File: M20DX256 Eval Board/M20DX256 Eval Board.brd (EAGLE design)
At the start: 60 x 30 mm, 20 parts, among them J1 M52-040000S0545, J2 20_PIN, J3 20_PIN, SW1 KMR211G, U1 MK20DX256VLH7, Y1 8MHz, Y2 32.768kHz, 12.5pF

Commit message: Place the component on the board
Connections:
- removed net XRES: U1.27
- net DAC0_OUT: now also J2.P$15; no longer J2.P$19
- net PGA0_N: now also J2.P$18; no longer J2.P$17
- net PGA0_P: now also J2.P$19; no longer J2.P$18
- net PGA1_N: now also J2.P$16; no longer J2.P$15
- net PGA1_P: now also J2.P$17; no longer J2.P$16
- net RESET: now also U1.27
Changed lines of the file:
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@@
 <wire x1="29.238" y1="9.3866" x2="52.185" y2="17.54" width="0" layer="19" extent="1-1"/>
-</signal>
-<signal name="XRES">
-<contactref element="U1" pad="27"/>
 </signal>
 <signal name="TMS/SWDIO">
@@
 <signal name="PGA1_N">
 <contactref element="U1" pad="12"/>
-<contactref element="J2" pad="P$15"/>
-<wire x1="18.57" y1="0" x2="24.3866" y2="13.2474" width="0" layer="19" extent="1-1"/>
+<contactref element="J2" pad="P$16"/>
+<wire x1="16.03" y1="0" x2="24.3866" y2="13.2474" width="0" layer="19" extent="1-1"/>
 </signal>
 <signal name="PGA1_P">
 <contactref element="U1" pad="11"/>
-<contactref element="J2" pad="P$16"/>
-<wire x1="16.03" y1="0" x2="24.3866" y2="13.7554" width="0" layer="19" extent="1-1"/>
+<contactref element="J2" pad="P$17"/>
+<wire x1="13.49" y1="0" x2="24.3866" y2="13.7554" width="0" layer="19" extent="1-1"/>
 </signal>
 <signal name="PGA0_N">
 <contactref element="U1" pad="10"/>
-<contactref element="J2" pad="P$17"/>
-<wire x1="13.49" y1="0" x2="24.3866" y2="14.238" width="0" layer="19" extent="1-1"/>
+<contactref element="J2" pad="P$18"/>
+<wire x1="10.95" y1="0" x2="24.3866" y2="14.238" width="0" layer="19" extent="1-1"/>
 </signal>
 <signal name="PGA0_P">
 <contactref element="U1" pad="9"/>
-<contactref element="J2" pad="P$18"/>
-<wire x1="10.95" y1="0" x2="24.3866" y2="14.746" width="0" layer="19" extent="1-1"/>
+<contactref element="J2" pad="P$19"/>
+<wire x1="8.41" y1="0" x2="24.3866" y2="14.746" width="0" layer="19" extent="1-1"/>
 </signal>
 <signal name="N$3">
@@
 <contactref element="SW1" pad="4"/>
 <contactref element="J1" pad="10"/>
+<contactref element="U1" pad="27"/>
 <wire x1="53.34" y1="9.31" x2="52.185" y2="16.27" width="0" layer="19" extent="1-1"/>
 <wire x1="53.34" y1="7.2" x2="53.34" y2="9.31" width="0" layer="19" extent="1-1"/>
@@
 <wire x1="56.4" y1="5.57" x2="53.34" y2="7.2" width="0" layer="19" extent="1-1"/>
 <wire x1="35.6134" y1="11.7488" x2="52.185" y2="16.27" width="0" layer="19" extent="1-1"/>
+<wire x1="31.2446" y1="9.3866" x2="35.6134" y2="11.7488" width="0" layer="19" extent="1-1"/>
 </signal>
 <signal name="N$7">
@@
 <signal name="DAC0_OUT">
 <contactref element="U1" pad="18"/>
-<contactref element="J2" pad="P$19"/>
-<wire x1="8.41" y1="0" x2="26.7488" y2="9.3866" width="0" layer="19" extent="1-1"/>
+<contactref element="J2" pad="P$15"/>
+<wire x1="18.57" y1="0" x2="26.7488" y2="9.3866" width="0" layer="19" extent="1-1"/>
 </signal>
 </signals>

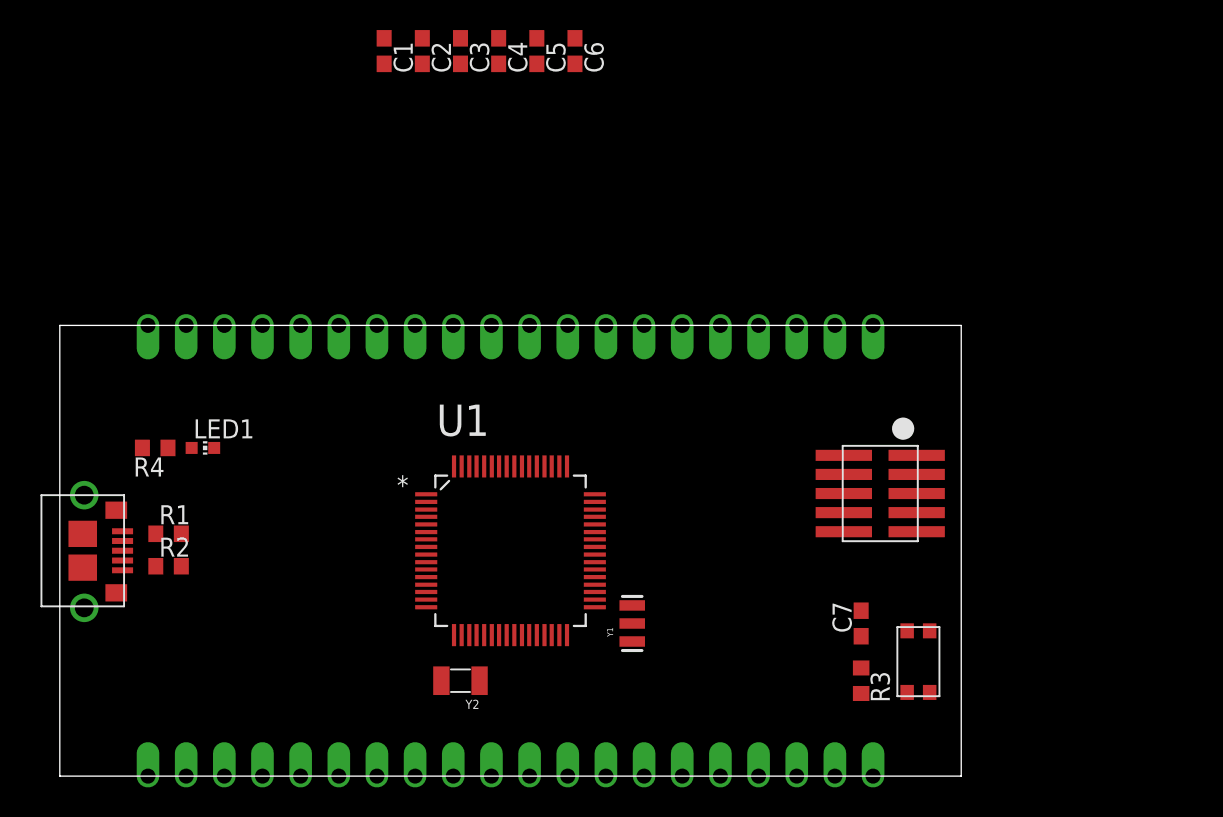
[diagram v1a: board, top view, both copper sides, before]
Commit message: route J3
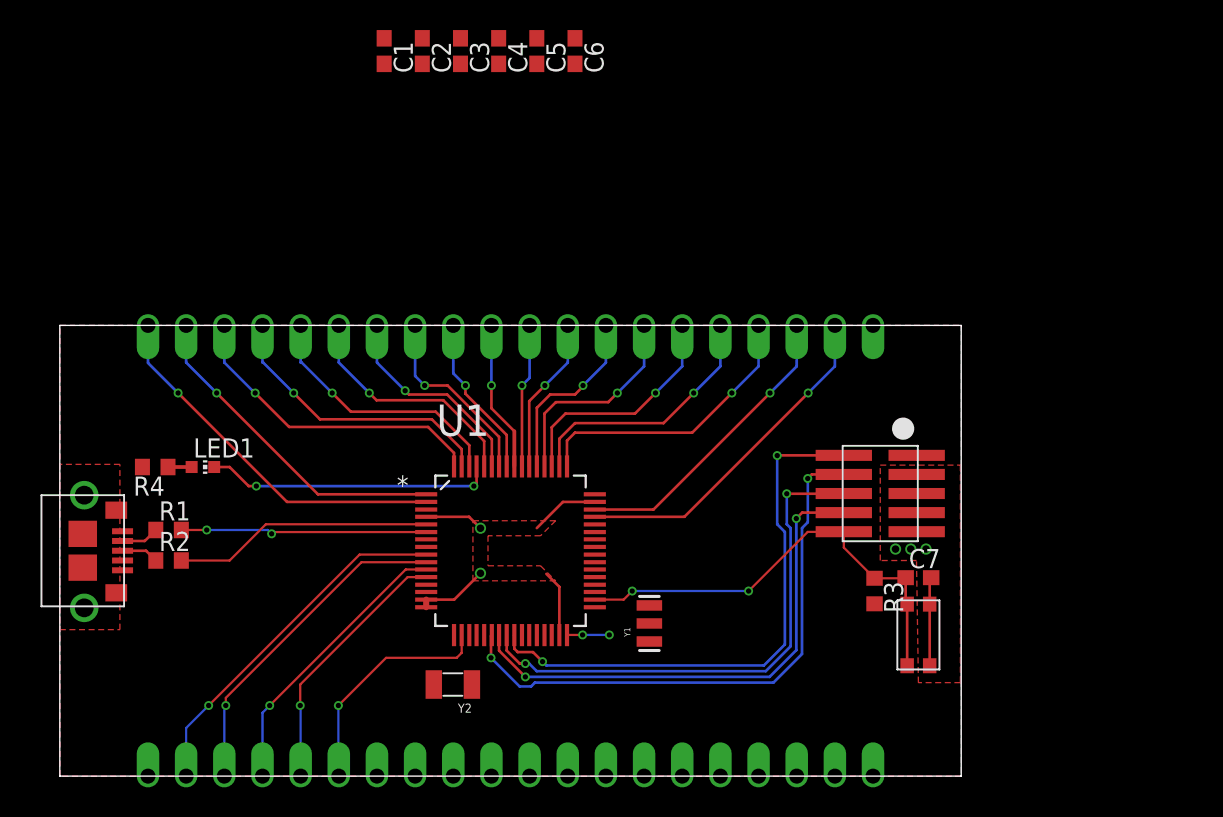
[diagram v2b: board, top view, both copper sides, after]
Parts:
- moved R3 6.03 mm to (54.2, 12.3)
- moved C7 4.88 mm to (57.1, 13.2), turned to 0 degrees
- moved SW1 1.78 mm to (57.1, 9.40)
- moved LED1 1.27 mm to (9.53, 20.6)
- moved R4 1.27 mm to (6.35, 20.6)
- moved Y1 1.14 mm to (39.2, 10.2)
- moved Y2 0.57 mm to (26.2, 6.10)
- moved R2 0.38 mm to (7.24, 14.4)
- moved R1 0.25 mm to (7.24, 16.4)
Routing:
- net TCK/SWDCLK: track 0.00 -> 38.3 mm, vias 0 -> 2
- net TMS/SWDIO: track 0.00 -> 37.2 mm, vias 0 -> 2
- net TDO: track 0.00 -> 35.2 mm, vias 0 -> 2
- net TDI: track 0.00 -> 34.4 mm, vias 0 -> 2
- net RESET: track 0.00 -> 30.4 mm, vias 0 -> 2
- net PTE1: track 0.00 -> 24.8 mm, vias 0 -> 1
- net PGA0_P: track 0.00 -> 24.0 mm, vias 0 -> 1
- net GND: track 0.00 -> 23.7 mm, vias 0 -> 5
- net PTC2: track 0.00 -> 22.8 mm, vias 0 -> 1
- net PGA0_N: track 0.00 -> 22.3 mm, vias 0 -> 1
- net PTE0: track 0.00 -> 22.1 mm, vias 0 -> 1
- net PTD7: track 0.00 -> 21.2 mm, vias 0 -> 1
- net PTC3: track 0.00 -> 20.1 mm, vias 0 -> 1
- net PTD6: track 0.00 -> 19.3 mm, vias 0 -> 1
- net PTC4: track 0.00 -> 19.2 mm, vias 0 -> 1
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- added copper zone on layer 1, net +3V3
- added copper zone on layer 1, net GND
- added copper zone on layer 16, net GND

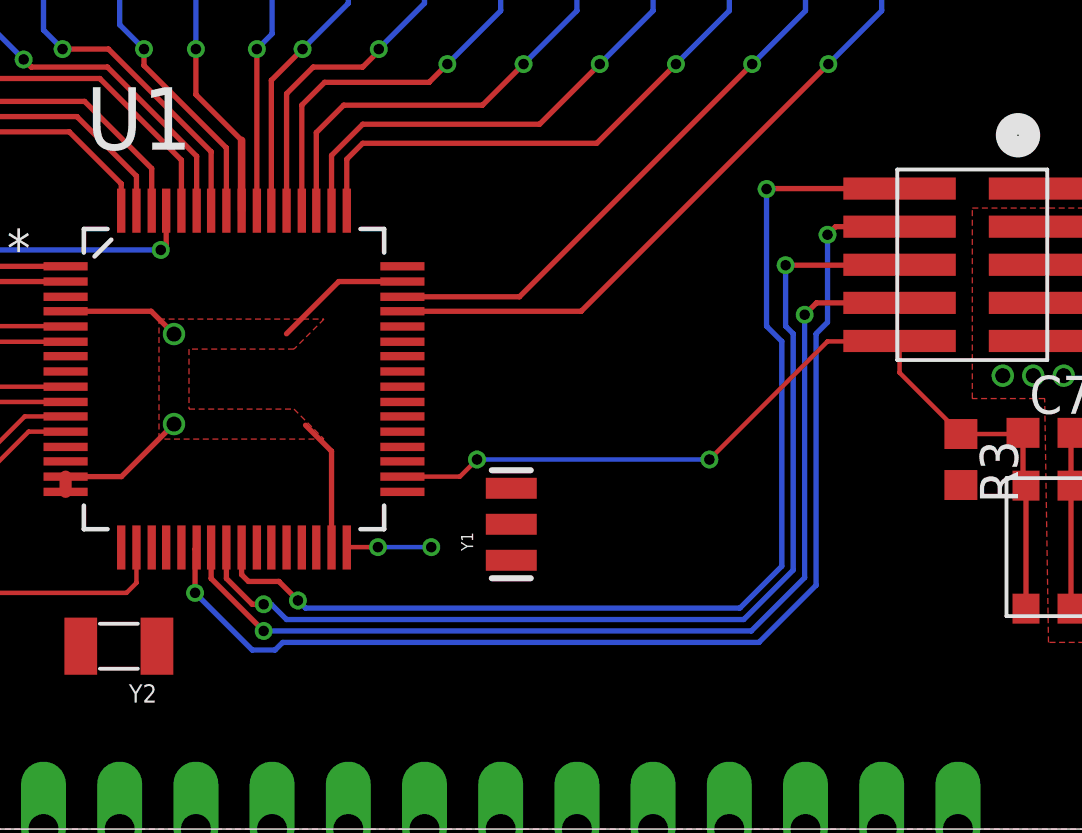
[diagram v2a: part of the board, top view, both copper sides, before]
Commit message: Route J1
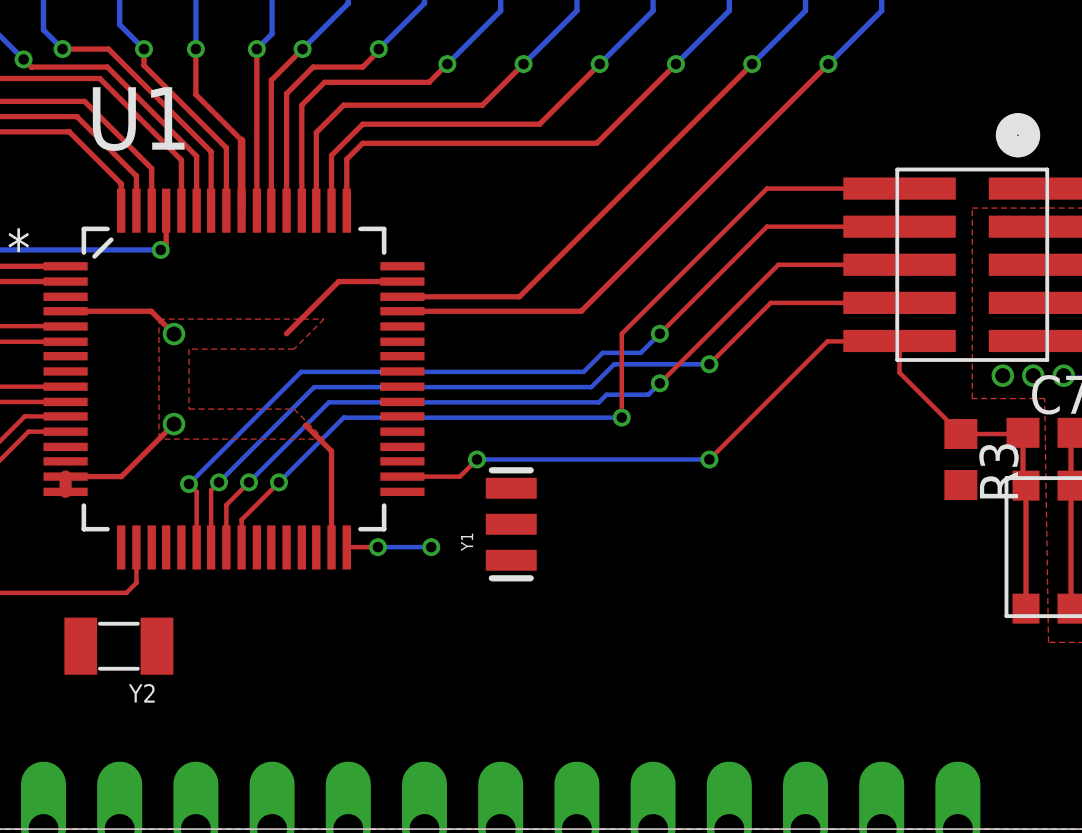
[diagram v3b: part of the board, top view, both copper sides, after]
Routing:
- net TCK/SWDCLK: track 38.3 -> 29.5 mm
- net TMS/SWDIO: track 37.2 -> 29.1 mm
- net TDO: track 35.2 -> 27.2 mm
- net TDI: track 34.4 -> 27.4 mm
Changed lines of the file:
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@@
 <contactref element="J1" pad="4"/>
 <contactref element="U1" pad="22"/>
-<wire x1="52.185" y1="20.08" x2="50.052" y2="20.08" width="0.1778" layer="1"/>
-<wire x1="50.052" y1="20.08" x2="49.784" y2="19.812" width="0.1778" layer="1"/>
-<via x="49.784" y="19.812" extent="1-16" drill="0.35"/>
-<wire x1="30.607" y1="5.969" x2="28.702" y2="7.874" width="0.1778" layer="16"/>
-<via x="28.702" y="7.874" extent="1-16" drill="0.35"/>
-<wire x1="28.702" y1="7.874" x2="28.702" y2="9.3332" width="0.1778" layer="1"/>
-<wire x1="28.702" y1="9.3332" x2="28.7554" y2="9.3866" width="0.1778" layer="1"/>
-<wire x1="49.784" y1="19.812" x2="49.784" y2="16.891" width="0.1778" layer="16"/>
-<wire x1="49.784" y1="16.891" x2="49.403" y2="16.51" width="0.1778" layer="16"/>
-<wire x1="49.403" y1="16.51" x2="49.403" y2="8.128" width="0.1778" layer="16"/>
-<wire x1="49.403" y1="8.128" x2="47.498" y2="6.223" width="0.1778" layer="16"/>
-<wire x1="30.607" y1="5.969" x2="31.369" y2="5.969" width="0.1778" layer="16"/>
-<wire x1="31.369" y1="5.969" x2="31.623" y2="6.223" width="0.1778" layer="16"/>
-<wire x1="31.623" y1="6.223" x2="47.498" y2="6.223" width="0.1778" layer="16"/>
+<via x="28.5" y="11.5" extent="1-16" drill="0.35"/>
+<wire x1="28.7554" y1="9.3866" x2="28.7554" y2="11.2446" width="0.15" layer="1"/>
+<wire x1="28.7554" y1="11.2446" x2="28.5" y2="11.5" width="0.15" layer="1"/>
+<wire x1="28.5" y1="11.5" x2="32.24" y2="15.24" width="0.15" layer="16"/>
+<wire x1="32.24" y1="15.24" x2="41.656" y2="15.24" width="0.15" layer="16"/>
+<via x="44.196" y="16.51" extent="1-16" drill="0.35"/>
+<wire x1="44.196" y1="16.51" x2="47.766" y2="20.08" width="0.15" layer="1"/>
+<wire x1="47.766" y1="20.08" x2="52.185" y2="20.08" width="0.15" layer="1"/>
+<wire x1="41.656" y1="15.24" x2="42.291" y2="15.875" width="0.15" layer="16"/>
+<wire x1="42.291" y1="15.875" x2="43.561" y2="15.875" width="0.15" layer="16"/>
+<wire x1="43.561" y1="15.875" x2="44.196" y2="16.51" width="0.15" layer="16"/>
 </signal>
 <signal name="TDO">
 <contactref element="J1" pad="6"/>
 <contactref element="U1" pad="24"/>
-<wire x1="29.746" y1="9.3866" x2="29.746" y2="8.354" width="0.1778" layer="1"/>
-<via x="30.988" y="7.493" extent="1-16" drill="0.35"/>
-<wire x1="30.988" y1="7.493" x2="31.242" y2="7.493" width="0.1778" layer="16"/>
-<wire x1="31.75" y1="6.985" x2="46.99" y2="6.985" width="0.1778" layer="16"/>
-<wire x1="46.99" y1="6.985" x2="48.641" y2="8.636" width="0.1778" layer="16"/>
-<wire x1="48.641" y1="8.636" x2="48.641" y2="16.51" width="0.1778" layer="16"/>
-<wire x1="48.641" y1="16.51" x2="48.387" y2="16.764" width="0.1778" layer="16"/>
-<wire x1="48.387" y1="16.764" x2="48.387" y2="18.796" width="0.1778" layer="16"/>
-<via x="48.387" y="18.796" extent="1-16" drill="0.35"/>
-<wire x1="48.387" y1="18.796" x2="52.171" y2="18.796" width="0.1778" layer="1"/>
+<via x="30.5" y="11.557" extent="1-16" drill="0.35"/>
 <wire x1="52.171" y1="18.796" x2="52.185" y2="18.81" width="0.1778" layer="1"/>
-<wire x1="30.988" y1="7.493" x2="30.607" y2="7.493" width="0.1778" layer="1"/>
-<wire x1="30.607" y1="7.493" x2="29.746" y2="8.354" width="0.1778" layer="1"/>
-<wire x1="31.242" y1="7.493" x2="31.75" y2="6.985" width="0.1778" layer="16"/>
+<wire x1="29.746" y1="9.3866" x2="29.746" y2="10.803" width="0.15" layer="1"/>
+<wire x1="29.746" y1="10.803" x2="30.5" y2="11.557" width="0.15" layer="1"/>
+<wire x1="30.5" y1="11.557" x2="33.167" y2="14.224" width="0.15" layer="16"/>
+<wire x1="33.167" y1="14.224" x2="42.164" y2="14.224" width="0.15" layer="16"/>
+<wire x1="42.164" y1="14.224" x2="42.418" y2="14.478" width="0.15" layer="16"/>
+<wire x1="42.418" y1="14.478" x2="43.815" y2="14.478" width="0.15" layer="16"/>
+<wire x1="43.815" y1="14.478" x2="44.196" y2="14.859" width="0.15" layer="16"/>
+<via x="44.196" y="14.859" extent="1-16" drill="0.35"/>
+<wire x1="44.196" y1="14.859" x2="48.147" y2="18.81" width="0.15" layer="1"/>
+<wire x1="48.147" y1="18.81" x2="52.185" y2="18.81" width="0.15" layer="1"/>
 </signal>
 <signal name="TDI">
 <contactref element="J1" pad="8"/>
 <contactref element="U1" pad="23"/>
-<wire x1="52.185" y1="17.54" x2="49.417" y2="17.54" width="0.1778" layer="1"/>
-<wire x1="49.417" y1="17.54" x2="49.022" y2="17.145" width="0.1778" layer="1"/>
-<via x="49.022" y="17.145" extent="1-16" drill="0.35"/>
-<wire x1="49.022" y1="17.145" x2="49.022" y2="8.382" width="0.1778" layer="16"/>
-<wire x1="49.022" y1="8.382" x2="47.244" y2="6.604" width="0.1778" layer="16"/>
-<wire x1="47.244" y1="6.604" x2="30.988" y2="6.604" width="0.1778" layer="16"/>
-<via x="30.988" y="6.604" extent="1-16" drill="0.35"/>
-<wire x1="30.988" y1="6.604" x2="29.238" y2="8.354" width="0.1778" layer="1"/>
-<wire x1="29.238" y1="8.354" x2="29.238" y2="9.3866" width="0.1778" layer="1"/>
+<via x="29.5" y="11.557" extent="1-16" drill="0.35"/>
+<wire x1="29.238" y1="9.3866" x2="29.238" y2="11.295" width="0.15" layer="1"/>
+<wire x1="29.238" y1="11.295" x2="29.5" y2="11.557" width="0.15" layer="1"/>
+<wire x1="29.5" y1="11.557" x2="32.675" y2="14.732" width="0.15" layer="16"/>
+<wire x1="32.675" y1="14.732" x2="41.91" y2="14.732" width="0.15" layer="16"/>
+<wire x1="41.91" y1="14.732" x2="42.672" y2="15.494" width="0.15" layer="16"/>
+<wire x1="42.672" y1="15.494" x2="45.847" y2="15.494" width="0.15" layer="16"/>
+<via x="45.847" y="15.494" extent="1-16" drill="0.35"/>
+<wire x1="45.847" y1="15.494" x2="47.893" y2="17.54" width="0.15" layer="1"/>
+<wire x1="47.893" y1="17.54" x2="52.185" y2="17.54" width="0.15" layer="1"/>
 </signal>
 <signal name="TMS/SWDIO">
 <contactref element="U1" pad="25"/>
 <contactref element="J1" pad="2"/>
-<via x="47.752" y="21.336" extent="1-16" drill="0.35"/>
-<via x="32.131" y="7.62" extent="1-16" drill="0.35"/>
+<via x="31.5" y="11.557" extent="1-16" drill="0.35"/>
 <wire x1="30.226" y1="9.3586" x2="30.254" y2="9.3866" width="0.1778" layer="1"/>
-<wire x1="30.254" y1="9.3866" x2="30.254" y2="8.481" width="0.1778" layer="1"/>
-<wire x1="30.254" y1="8.481" x2="30.48" y2="8.255" width="0.1778" layer="1"/>
-<wire x1="30.48" y1="8.255" x2="31.496" y2="8.255" width="0.1778" layer="1"/>
-<wire x1="31.496" y1="8.255" x2="32.131" y2="7.62" width="0.1778" layer="1"/>
-<wire x1="32.131" y1="7.62" x2="32.385" y2="7.366" width="0.1778" layer="16"/>
-<wire x1="32.385" y1="7.366" x2="46.863" y2="7.366" width="0.1778" layer="16"/>
-<wire x1="46.863" y1="7.366" x2="48.26" y2="8.763" width="0.1778" layer="16"/>
-<wire x1="48.26" y1="8.763" x2="48.26" y2="16.256" width="0.1778" layer="16"/>
-<wire x1="48.26" y1="16.256" x2="47.752" y2="16.764" width="0.1778" layer="16"/>
-<wire x1="47.752" y1="16.764" x2="47.752" y2="21.336" width="0.1778" layer="16"/>
-<wire x1="47.752" y1="21.336" x2="47.766" y2="21.35" width="0.1778" layer="1"/>
-<wire x1="47.766" y1="21.35" x2="52.185" y2="21.35" width="0.1778" layer="1"/>
-<wire x1="47.752" y1="21.336" x2="47.752" y2="21.35" width="0.1778" layer="16"/>
+<wire x1="30.254" y1="9.3866" x2="30.254" y2="10.311" width="0.15" layer="1"/>
+<wire x1="30.254" y1="10.311" x2="31.5" y2="11.557" width="0.15" layer="1"/>
+<wire x1="31.5" y1="11.557" x2="33.659" y2="13.716" width="0.15" layer="16"/>
+<wire x1="33.659" y1="13.716" x2="42.926" y2="13.716" width="0.15" layer="16"/>
+<via x="42.926" y="13.716" extent="1-16" drill="0.35"/>
+<wire x1="42.926" y1="13.716" x2="42.926" y2="16.51" width="0.15" layer="1"/>
+<wire x1="42.926" y1="16.51" x2="47.766" y2="21.35" width="0.15" layer="1"/>
+<wire x1="47.766" y1="21.35" x2="52.185" y2="21.35" width="0.15" layer="1"/>
 </signal>
 <signal name="PTB0">

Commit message: route J2
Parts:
- moved C5 47.0 mm to (72.8, 25.3)
- moved C4 44.4 mm to (67.3, 25.4)
- moved C3 38.9 mm to (19.9, 9.91), turned to 90 degrees
- moved C2 38.4 mm to (22.1, 9.91), turned to 90 degrees
- moved C1 30.7 mm to (21.0, 17.5), turned to 0 degrees
- moved C6 28.8 mm to (38.2, 19.7)
- moved Y1 5.85 mm to (34.4, 6.86), turned to 0 degrees
- moved Y2 0.52 mm to (25.7, 6.22)
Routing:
- net PTC1: track 0.00 -> 26.5 mm, vias 0 -> 1
- net PTC0: track 0.00 -> 24.8 mm, vias 0 -> 1
- net PTB19: track 0.00 -> 23.2 mm, vias 0 -> 1
- net PTB0: track 0.00 -> 22.3 mm, vias 0 -> 1
- net PTB1: track 0.00 -> 21.6 mm, vias 0 -> 1
- net PTB18: track 0.00 -> 21.6 mm, vias 0 -> 1
- net PTB2: track 0.00 -> 20.5 mm, vias 0 -> 1
- net PTB5: track 0.00 -> 19.9 mm, vias 0 -> 1
- net PTB4: track 0.00 -> 19.9 mm, vias 0 -> 1
- net PTB3: track 0.00 -> 19.8 mm, vias 0 -> 1
- net PTA4: track 0.00 -> 17.1 mm, vias 0 -> 1
- net PTA12: track 0.00 -> 15.5 mm, vias 0 -> 1
- net GND: track 23.7 -> 38.6 mm, vias 5 -> 7
- net PTA13: track 0.00 -> 13.1 mm, vias 0 -> 1
- net RESET: track 30.4 -> 40.8 mm, vias 2 -> 3
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
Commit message: Route the power supply +5V
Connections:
- net +5V: now also J2.P$20; no longer J3.P$20
- net GND: now also J3.P$20; no longer J2.P$20
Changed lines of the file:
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@@
 <contactref element="SW1" pad="1"/>
 <contactref element="Y1" pad="2"/>
-<contactref element="J2" pad="P$20"/>
 <polygon width="0.4064" layer="16">
 <vertex x="0" y="30"/>
@@
 <wire x1="35.6134" y1="18.2512" x2="37.6432" y2="18.2512" width="0.1778" layer="1"/>
 <wire x1="37.6432" y1="18.2512" x2="38.227" y2="18.835" width="0.1778" layer="1"/>
+<contactref element="J3" pad="P$20"/>
 <wire x1="67.31" y1="24.55" x2="72.771" y2="24.423" width="0" layer="19" extent="1-1"/>
 <wire x1="57.035" y1="20.08" x2="67.31" y2="24.55" width="0" layer="19" extent="1-1"/>
+<wire x1="54.13" y1="30" x2="57.035" y2="20.08" width="0" layer="19" extent="1-1"/>
 </signal>
 <signal name="+5V">
 <contactref element="U$1" pad="1"/>
 <contactref element="U1" pad="8"/>
-<contactref element="J3" pad="P$20"/>
-<wire x1="24.3866" y1="15.254" x2="54.13" y2="30" width="0" layer="19" extent="1-1"/>
+<contactref element="J2" pad="P$20"/>
 <wire x1="4.177" y1="16.3" x2="24.3866" y2="15.254" width="0" layer="19" extent="1-1"/>
+<wire x1="5.87" y1="0" x2="4.177" y2="16.3" width="0" layer="19" extent="1-1"/>
 </signal>
 <signal name="N$1">
